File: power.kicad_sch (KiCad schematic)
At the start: 80 parts, among them IC1 STM32MP157AAB3, IC3 STC3117IJT, IC4 MCP73830T-2AAI_MYY, IC5 MT41K256M16TW-107_P, IC6 STPMIC1BPQR, IC8 STUSB1600AQTR, J1 Conn_01x04, P1 USB_C_Plug_USB2.0, Q1 PMDPB70XP_115

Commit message: cleanup schematic
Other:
- note added: "VBAT other uses: Seems like this pin is used if you want to power it throug a battery. However, we already power our whole circuit through a battery + regulators. So connect regulators should be perfectly fine. VBAT must be in range 1.2 - 3.6V"
- note added: "changed to 1V8 use BUCK4, since it can supply 2A"
- note added: "changed to 3V3 used for STUSB VSYS (3V-5V)"
- note removed: "TODO: change to 1V8 use BUCK4, since it can supply 2A"
- note removed: "VBAT other uses: Seems like this pin is used if you want to power it throug a battery. However, we already power our whole circuit through a battery + regulators. So connect regulators should be perfectly fine."
- note removed: "used for STUSB VSYS (3V-5V)"
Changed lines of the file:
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@@
     (effects (font (size 1.27 1.27)) (justify left bottom))
   )
-  (text "used for STUSB VSYS (3V-5V)" (at 115.57 209.55 0)
+  (text "changed to 3V3\nused for STUSB VSYS (3V-5V)" (at 123.19 209.55 0)
     (effects (font (size 1.27 1.27) (color 255 0 24 1)) (justify left bottom))
   )
@@
     (effects (font (size 1.27 1.27)) (justify left bottom))
   )
-  (text "VBAT other uses:\n\nSeems like this pin is used if you want to power it throug a battery.\nHowever, we already power our whole circuit through a battery + regulators.\n\nSo connect regulators should be perfectly fine."
-    (at 252.73 281.94 0)
+  (text "VBAT other uses:\n\nSeems like this pin is used if you want to power it throug a battery.\nHowever, we already power our whole circuit through a battery + regulators.\n\nSo connect regulators should be perfectly fine.\n\nVBAT must be in range 1.2 - 3.6V"
+    (at 252.73 285.75 0)
     (effects (font (size 1.27 1.27)) (justify left bottom))
   )
@@
     (effects (font (size 1.27 1.27) (color 255 0 24 1)) (justify left bottom))
   )
-  (text "TODO: change to 1V8\nuse BUCK4, since it can supply 2A"
-    (at 124.46 231.14 0)
+  (text "changed to 1V8\nuse BUCK4, since it can supply 2A" (at 124.46 231.14 0)
     (effects (font (size 1.27 1.27) (color 255 0 24 1)) (justify left bottom))
   )

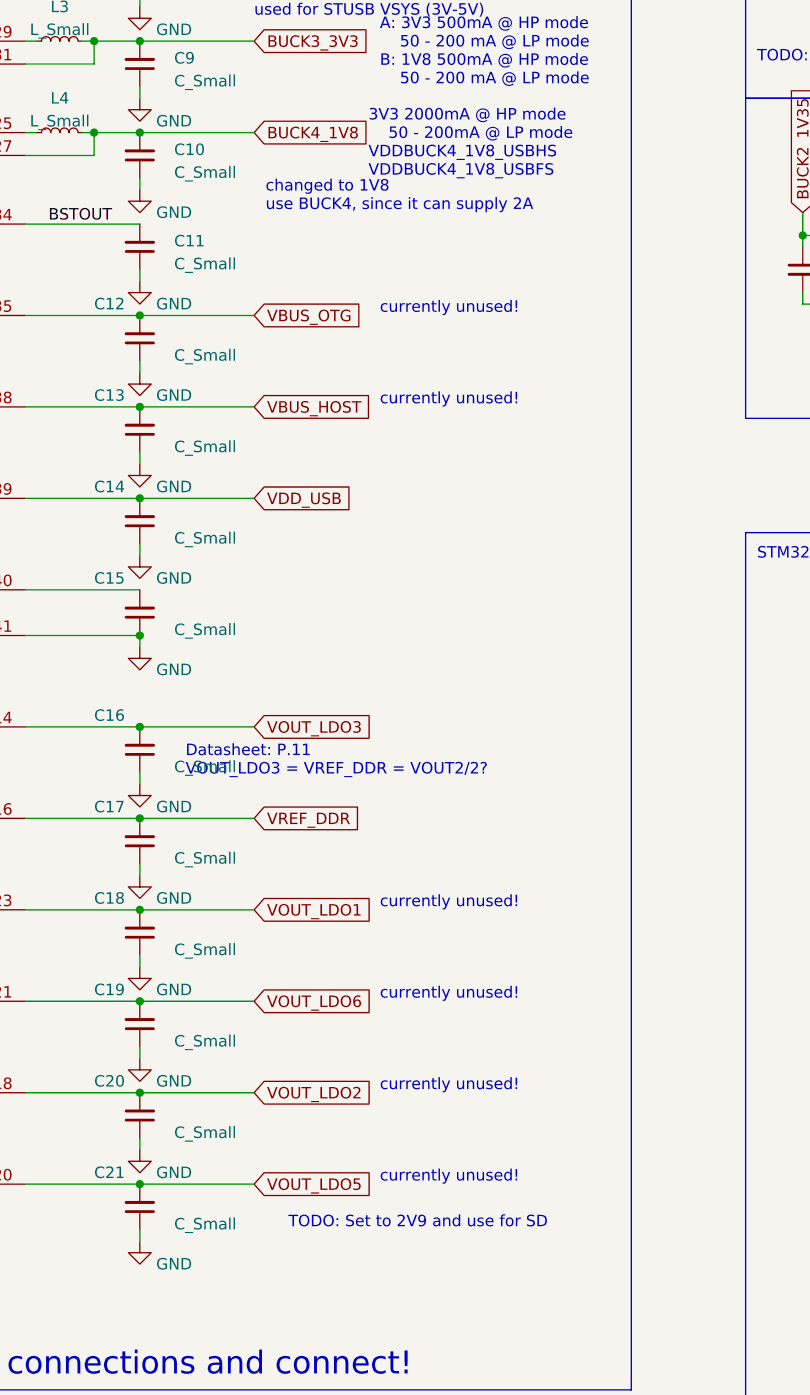
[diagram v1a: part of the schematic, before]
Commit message: Add SDCard connection to mpu
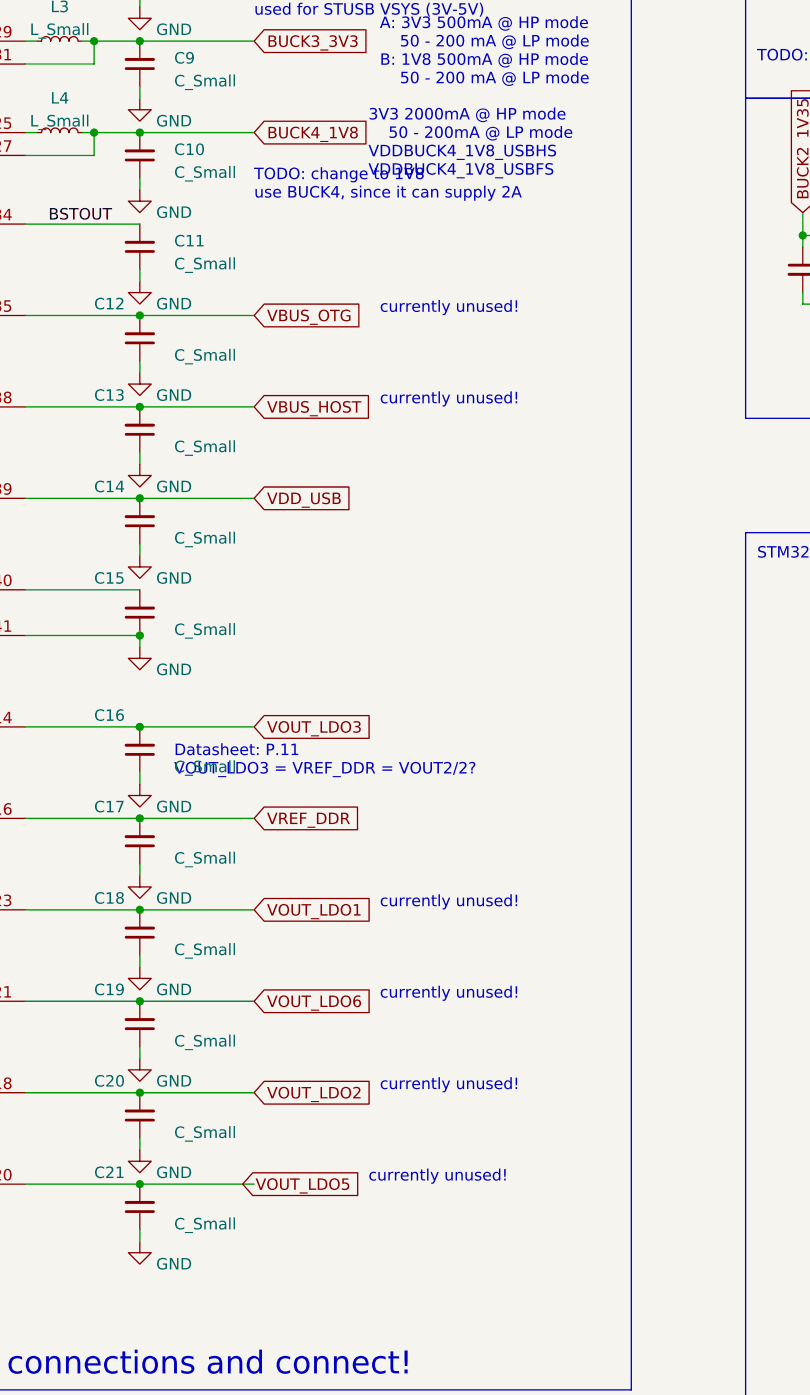
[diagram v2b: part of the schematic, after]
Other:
- note added: "TODO: change to 1V8 use BUCK4, since it can supply 2A"
- note removed: "TODO: Set to 2V9 and use for SD"
- note removed: "changed to 1V8 use BUCK4, since it can supply 2A"
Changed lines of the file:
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@@
-    (effects (font (size 1.27 1.27)) (justify left bottom))
-  )
-  (text "TODO: Set to 2V9 and use for SD" (at 127 344.17 0)
     (effects (font (size 1.27 1.27)) (justify left bottom))
   )
@@
     (effects (font (size 1.27 1.27)) (justify left bottom))
   )
-  (text "Datasheet: P.11\nVOUT_LDO3 = VREF_DDR = VOUT2/2?\n\n" (at 115.57 295.91 0)
+  (text "Datasheet: P.11\nVOUT_LDO3 = VREF_DDR = VOUT2/2?\n\n" (at 114.3 295.91 0)
     (effects (font (size 1.27 1.27)) (justify left bottom))
   )
@@
     (effects (font (size 1.27 1.27)) (justify left bottom))
   )
-  (text "currently unused!" (at 137.16 339.09 0)
-    (effects (font (size 1.27 1.27) (color 255 0 24 1)) (justify left bottom))
-  )
-  (text "changed to 1V8\nuse BUCK4, since it can supply 2A" (at 124.46 231.14 0)
+  (text "currently unused!" (at 135.89 339.09 0)
+    (effects (font (size 1.27 1.27) (color 255 0 24 1)) (justify left bottom))
+  )
+  (text "TODO: change to 1V8\nuse BUCK4, since it can supply 2A"
+    (at 123.19 229.87 0)
     (effects (font (size 1.27 1.27) (color 255 0 24 1)) (justify left bottom))
   )
@@
     )
   )
-  (global_label "VOUT_LDO5" (shape input) (at 123.19 339.09 0) (fields_autoplaced)
+  (global_label "VOUT_LDO5" (shape input) (at 121.92 339.09 0) (fields_autoplaced)
     (effects (font (size 1.27 1.27)) (justify left))
     (property "Intersheetrefs" "${INTERSHEET_REFS}" (at 136.6187 339.09 0)

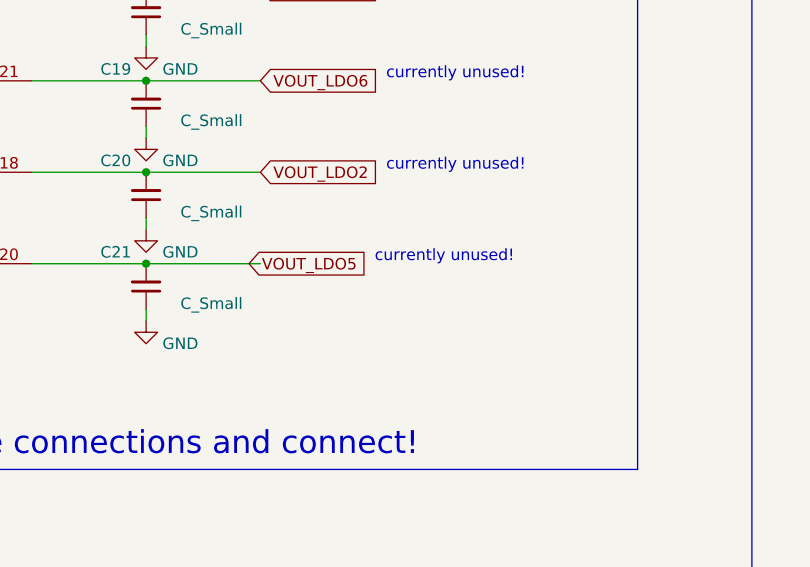
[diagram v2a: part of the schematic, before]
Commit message: Add SDCard Label
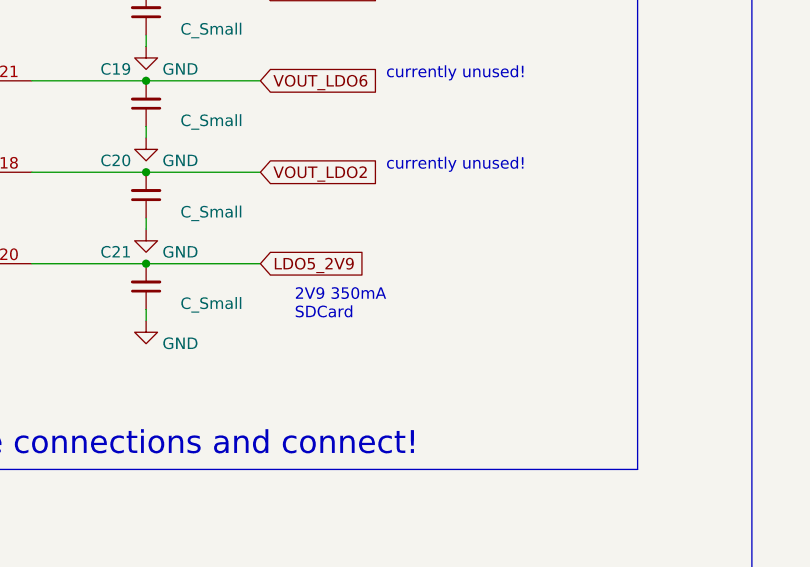
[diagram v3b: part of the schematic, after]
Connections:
- net VOUT_LDO5 renamed LDO5_2V9
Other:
- note added: "2V9 350mA SDCard"
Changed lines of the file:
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@@
     (effects (font (size 1.27 1.27) (color 255 0 24 1)) (justify left bottom))
+  )
+  (text "2V9 350mA\nSDCard" (at 127 345.44 0)
+    (effects (font (size 1.27 1.27)) (justify left bottom))
   )
   (text "TODO" (at 334.01 138.43 0)
@@
     (effects (font (size 1.27 1.27)) (justify left bottom))
   )
-  (text "currently unused!" (at 135.89 339.09 0)
-    (effects (font (size 1.27 1.27) (color 255 0 24 1)) (justify left bottom))
-  )
   (text "TODO: change to 1V8\nuse BUCK4, since it can supply 2A"
     (at 123.19 229.87 0)
@@
     )
   )
+  (global_label "LDO5_2V9" (shape input) (at 123.19 339.09 0) (fields_autoplaced)
+    (effects (font (size 1.27 1.27)) (justify left))
+    (property "Intersheetrefs" "${INTERSHEET_REFS}" (at 136.6187 339.09 0)
+      (effects (font (size 1.27 1.27)) (justify left) hide)
+    )
+  )
   (global_label "BUCK4_1V8" (shape input) (at 359.41 311.15 90) (fields_autoplaced)
     (effects (font (size 1.27 1.27)) (justify left))
@@
       (effects (font (size 1.27 1.27)) (justify left) hide)
     )
-  )
-  (global_label "VOUT_LDO5" (shape input) (at 121.92 339.09 0) (fields_autoplaced)
-    (effects (font (size 1.27 1.27)) (justify left))
-    (property "Intersheetrefs" "${INTERSHEET_REFS}" (at 136.6187 339.09 0)
-      (effects (font (size 1.27 1.27)) (justify left) hide)
-    )

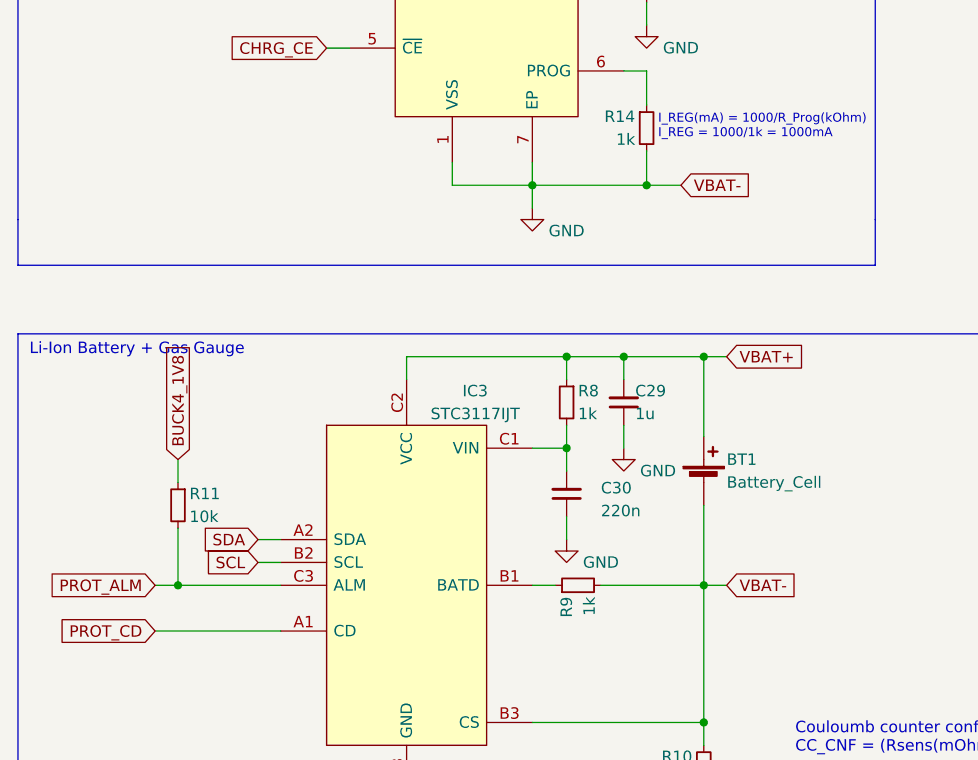
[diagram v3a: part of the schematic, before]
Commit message: added footprint for nRF, changed symbol background color, checked connections
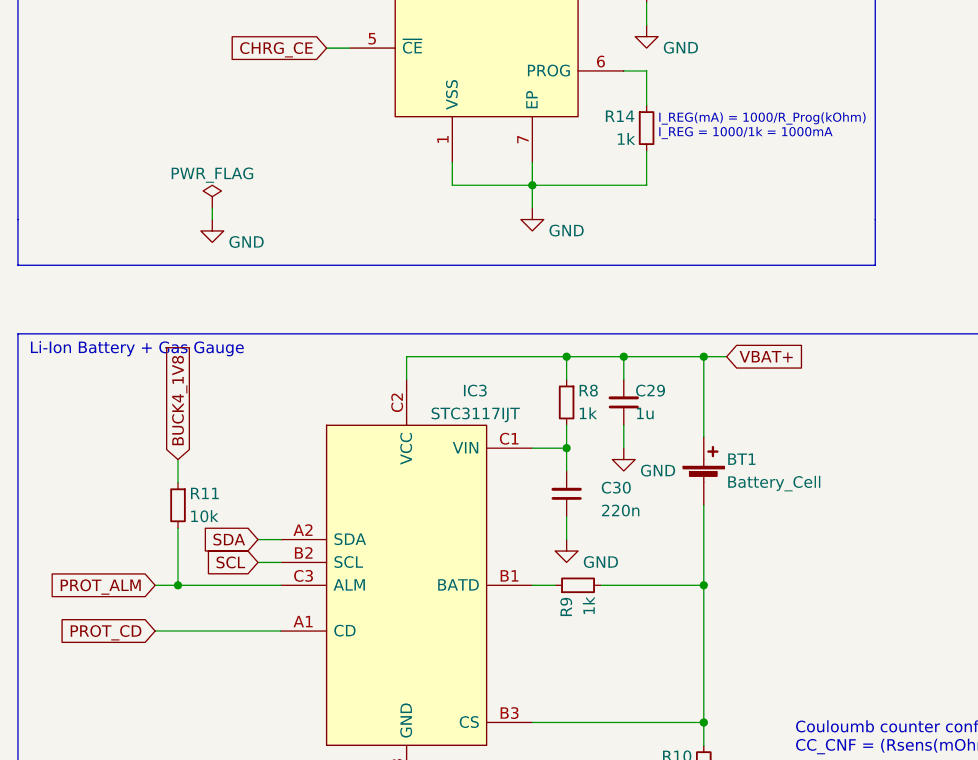
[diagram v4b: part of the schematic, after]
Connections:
- net GND: no longer BT1.2 (-), IC3.B3 (CS), R10.2, R9.2
- new net: BT1.2 (-), IC3.B3 (CS), R10.2, R9.2
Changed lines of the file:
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@@
   (junction (at 43.18 224.79) (diameter 0) (color 0 0 0 0)
   )
-  (junction (at 323.85 72.39) (diameter 0) (color 0 0 0 0)
-  )
   (junction (at 340.36 201.93) (diameter 0) (color 0 0 0 0)
   )
@@
     (stroke (width 0) (type default))
   )
+  (wire (pts (xy 275.59 74.93) (xy 275.59 76.2))
+    (stroke (width 0) (type default))
+  )
   (wire (pts (xy 281.94 30.48) (xy 306.07 30.48))
     (stroke (width 0) (type default))
@@
     (stroke (width 0) (type default))
   )
-  (wire (pts (xy 323.85 72.39) (xy 327.66 72.39))
-    (stroke (width 0) (type default))
-  )
   (wire (pts (xy 311.15 72.39) (xy 311.15 74.93))
     (stroke (width 0) (type default))
@@
     (stroke (width 0) (type default))
   )
-  (wire (pts (xy 330.2 116.84) (xy 332.74 116.84))
-    (stroke (width 0) (type default))
-  )
   (wire (pts (xy 110.49 318.77) (xy 123.19 318.77))
     (stroke (width 0) (type default))
@@
     )
   )
-  (global_label "VBAT-" (shape input) (at 332.74 116.84 0) (fields_autoplaced)
-    (effects (font (size 1.27 1.27)) (justify left))
-    (property "Intersheetrefs" "${INTERSHEET_REFS}" (at 341.633 116.84 0)
-      (effects (font (size 1.27 1.27)) (justify left) hide)
-    )
-  )
   (global_label "BUCK1_1V2" (shape input) (at 123.19 191.77 0) (fields_autoplaced)
     (effects (font (size 1.27 1.27)) (justify left))
@@
     )
   )
-  (global_label "VBAT-" (shape input) (at 327.66 72.39 0) (fields_autoplaced)
-    (effects (font (size 1.27 1.27)) (justify left))
-    (property "Intersheetrefs" "${INTERSHEET_REFS}" (at 336.553 72.39 0)
-      (effects (font (size 1.27 1.27)) (justify left) hide)
-    )
-  )
   (global_label "BUCK1_1V2" (shape input) (at 267.97 306.07 90) (fields_autoplaced)
     (effects (font (size 1.27 1.27)) (justify left))
@@
     )
   )
+  (symbol (lib_id "power:PWR_FLAG") (at 275.59 74.93 0) (unit 1)
+    (in_bom yes) (on_board yes) (dnp no) (fields_autoplaced)
+    (property "Reference" "#FLG01" (at 275.59 73.025 0)
+      (effects (font (size 1.27 1.27)) hide)
+    )
+    (property "Value" "PWR_FLAG" (at 275.59 71.12 0)
+      (effects (font (size 1.27 1.27)))
+    )
+    (property "Footprint" "" (at 275.59 74.93 0)
+      (effects (font (size 1.27 1.27)) hide)
+    )
+    (property "Datasheet" "~" (at 275.59 74.93 0)
+      (effects (font (size 1.27 1.27)) hide)
+    )
+    (pin "1")
+    (instances
+      (project "gba"
+        (path "/017c50c6-333c-4d31-ad5a-278994a09b14/5731d22b-18c2-4920-9f80-2a6ce209edf2"
+          (reference "#FLG01") (unit 1)
+        )
+      )
+    )
+  )
   (symbol (lib_id "Device:C_Small") (at 184.15 237.49 0) (unit 1)
     (in_bom yes) (on_board yes) (dnp no) (fields_autoplaced)
@@
         )
       )
+    )
+  )
+  (symbol (lib_id "power:GND") (at 275.59 76.2 0) (unit 1)
+    (in_bom yes) (on_board yes) (dnp no)
+    (property "Reference" "#PWR073" (at 275.59 82.55 0)
+      (effects (font (size 1.27 1.27)) hide)
+    )
+    (property "Value" "GND" (at 279.4 78.74 0)
+      (effects (font (size 1.27 1.27)))
+    )
+    (property "Footprint" "" (at 275.59 76.2 0)
+      (effects (font (size 1.27 1.27)) hide)
+    )
+    (property "Datasheet" "" (at 275.59 76.2 0)
+      (effects (font (size 1.27 1.27)) hide)
+    )
+    (pin "1")
+    (instances
+      (project "gba"
+        (path "/017c50c6-333c-4d31-ad5a-278994a09b14/5731d22b-18c2-4920-9f80-2a6ce209edf2"
+          (reference "#PWR073") (unit 1)
+        )
+      )
